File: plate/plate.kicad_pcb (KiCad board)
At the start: 2 copper layers, 299.5 x 123 mm, 73 parts

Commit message: M  border.py M  plate/plate.kicad_pcb
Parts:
- moved S62 1.04 mm to (74.6, 78.0), turned to -10 degrees
- moved S68 0.86 mm to (198.3, 77.7), turned to 10 degrees
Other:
- board size 299.5 x 123 mm -> 299.2 x 122.8 mm

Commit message: M  border.py M  place.py M  plate/plate.kicad_pcb M  plate/plate.kicad_sch
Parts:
- S29, S41, S63: footprint tmr-lib:Switch_Cutout2_MX_1.25u -> tmr-lib:Switch_Cutout2_MX
- S30, S42, S45: footprint tmr-lib:Switch_Cutout2_MX -> tmr-lib:Switch_Cutout2_MX_1.25u
- moved S63 2.32 mm to (95.6, 86.0), turned to -20 degrees
- moved S62 2.24 mm to (73.6, 76.0), turned to 0 degrees
- moved S68 2.08 mm to (199.5, 76.0), turned to 0 degrees
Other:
- board size 299.2 x 122.8 mm -> 299.5 x 123 mm

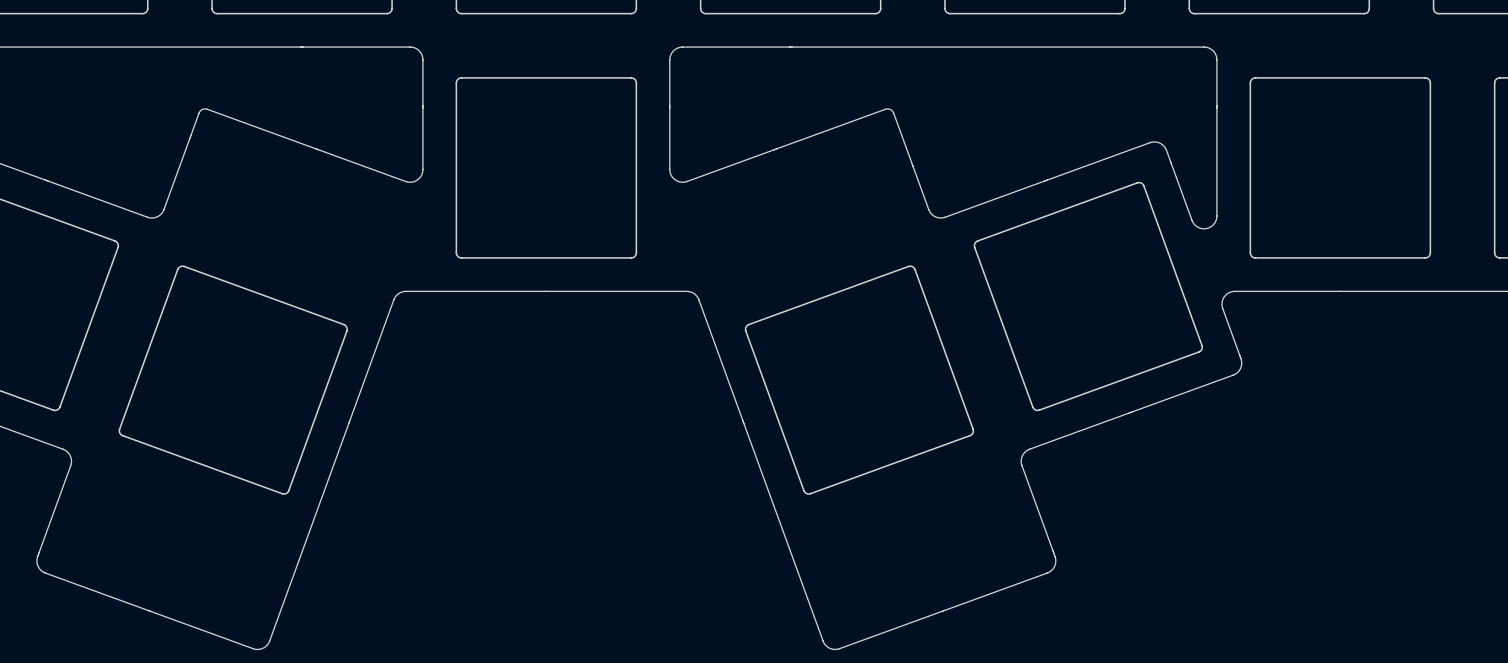
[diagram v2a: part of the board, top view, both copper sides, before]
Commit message: A  RP2040_Minimal.kicad_sym A  RP2040_minimal.pretty/8-USON-Handsolder.kicad_mod A  RP2040_minimal.pretty/8-USON.kicad_mod A  RP2040_minimal.pretty/C_0402_1005Metric.kicad_mod A  RP2040_minimal.pretty/C_0603_1608Metric.kicad_mod A  RP2040_minimal.pretty/C_0603_1608Metric_Pad1.08x0.95mm_HandSolder.kicad_mod A  RP2040_minimal.pretty/C_1206_3216Metric.kicad_mod A  RP2040_minimal.pretty/Crystal_SMD_2520-4Pin_2.5x2.0mm-Handsolder.kicad_mod A  RP2040_minimal.pretty/Crystal_SMD_HC49-US.kicad_mod A  RP2040_minimal.pretty/D_0402_1005Metric.kicad_mod A  RP2040_minimal.pretty/D_SOD-523.kicad_mod A  RP2040_minimal.pretty/Diodes_U_DFN1212_3.kicad_mod A  RP2040_minimal.pretty/Diodes_U_DFN1212_3_Handsolder.kicad_mod A  RP2040_minimal.pretty/LED_0402_1005Metric.kicad_mod A  RP2040_minimal.pretty/LED_Driver_Mod_Conn.kicad_mod A  RP2040_minimal.pretty/LED_Driver_Mod_Conn_1.27.kicad_mod A  RP2040_minimal.pretty/Module_Conn_Regular.kicad_mod A  RP2040_minimal.pretty/Module_Conn_Regular2.kicad_mod A  RP2040_minimal.pretty/Module_Conn_Regular_Outline.kicad_mod A  RP2040_minimal.pretty/QFN-28-1EP_4x4mm_P0.4mm_EP2.3x2.3mm-Handsolder.kicad_mod A  RP2040_minimal.pretty/QFN-28-1EP_4x4mm_P0.4mm_EP2.3x2.3mm.kicad_mod A  RP2040_minimal.pretty/RP2040-QFN-56-Handsolder.kicad_mod A  RP2040_minimal.pretty/RP2040-QFN-56.kicad_mod A  RP2040_minimal.pretty/R_0402_1005Metric.kicad_mod A  RP2040_minimal.pretty/R_0603_1608Metric_Pad0.98x0.95mm_HandSolder.kicad_mod A  RP2040_minimal.pretty/SW_CK_KXT3.kicad_mod A  RP2040_minimal.pretty/SW_SPST_Panasonic_EVPAF.kicad_mod A  RP2040_minimal.pretty/SW_Side_EVPAV.kicad_mod A  RP2040_minimal.pretty/SW_XKB_TS_2030.kicad_mod A  RP2040_minimal.pretty/USB_Micro-B_Amphenol_10103594-0001LF_Horizontal_modified.kicad_mod A  RP2040_minimal.pretty/XSON-8-1EP_4x4mm.kicad_mod M  border.py M  notes/notes.md M  pcb/fp-lib-table M  pcb/pcb.kicad_pcb M  pcb/pcb.kicad_prl M  pcb/pcb.kicad_sch M  plate/plate.kicad_pcb M  plate/plate.kicad_sch R  tmr-footprints/Switch_Cutout2_MX.kic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
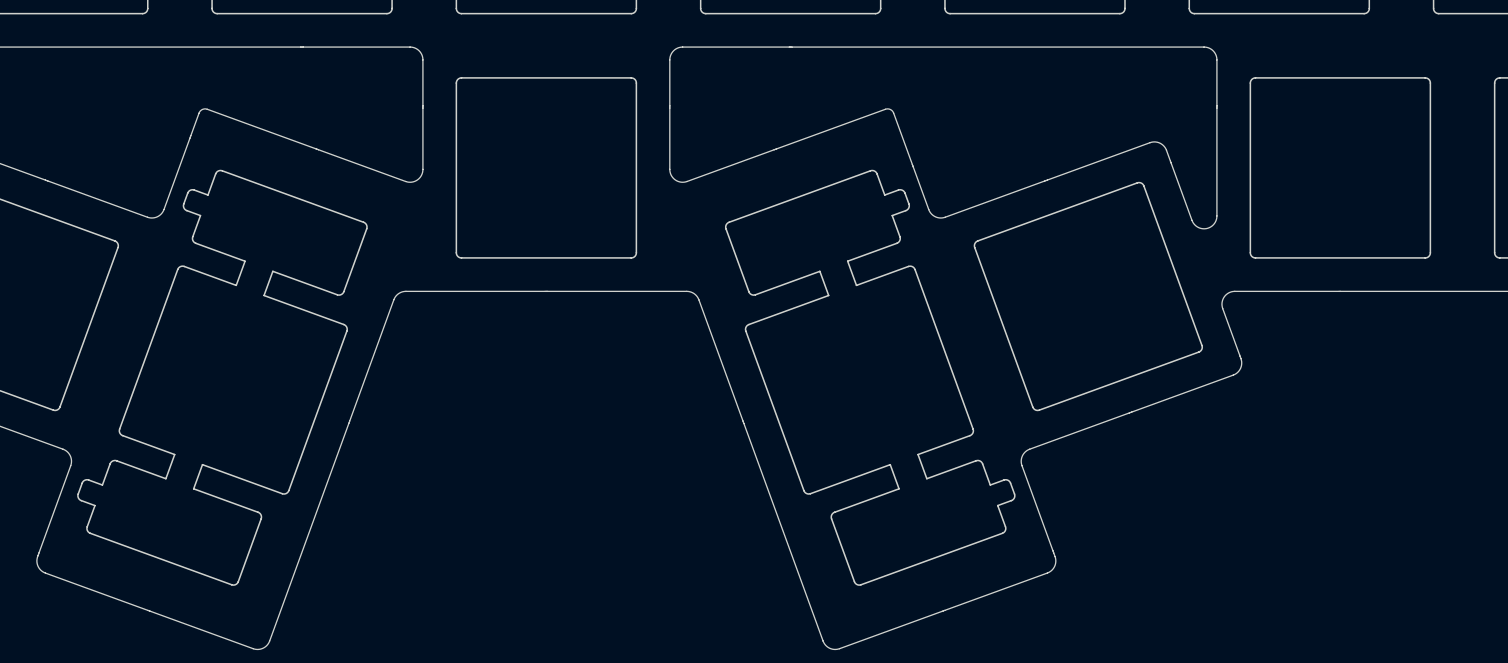
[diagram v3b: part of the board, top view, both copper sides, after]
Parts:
- S1, S10, S11, S12, S13, S14, S15, S16, S17, S18, S19, S2, S20, S21, S22, S23, S24, S25, S26, S27, S28, S29, S3, S31, S32, S33, S34, S35, S36, S37, S38, S39, S4, S40, S41, S43, S44, S47, S48, S49, S5, S50, S51, S52, S53, S54, S55, S56, S58, S6, S61, S63, S65, S67, S68, S69, S7, S71, S72, S8, S9: footprint tmr-lib:Switch_Cutout2_MX -> tmr-lib:Switch_Cutout
- S30, S42, S45, S59, S60, S62, S70: footprint tmr-lib:Switch_Cutout2_MX_1.25u -> tmr-lib:Switch_Cutout_1.25u
- S46, S57: footprint tmr-lib:Switch_Cutout2_MX_1.75u -> tmr-lib:Switch_Cutout_1.75u
- S64, S66: footprint tmr-lib:Switch_Cutout2_MX_2u -> tmr-lib:Switch_Cutout_2u

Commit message: M  border.py M  notes/components.md A  notes/mcu M  pcb/pcb.kicad_pcb M  place.py M  plate/plate.kicad_pcb M  plate/plate.kicad_sch
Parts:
- S1: footprint tmr-lib:Switch_Cutout -> tmr-lib:Switch_Cutout_1.25u
- S62: footprint tmr-lib:Switch_Cutout_1.25u -> tmr-lib:Switch_Cutout
- moved S62 5.32 mm to (77.6, 79.5), turned to -20 degrees
- moved S59 4.15 mm to (11.3, 76.0)
- moved S60 4.15 mm to (35.0, 76.0)
- moved S61 4.15 mm to (56.4, 76.0)
- moved S68 3.91 mm to (197.8, 79.5), turned to 20 degrees
- moved S1 2.38 mm to (16.6, 0.00)
- moved S71 0.60 mm to (261.9, 76.0)
- moved S72 0.60 mm to (280.9, 76.0)
- moved S69 0.60 mm to (219.1, 76.0)
- moved S70 0.60 mm to (240.5, 76.0)
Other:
- board size 299.5 x 123 mm -> 299 x 122.8 mm
